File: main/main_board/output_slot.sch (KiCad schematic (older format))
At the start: 5 parts, among them P1 my_pcie_8x

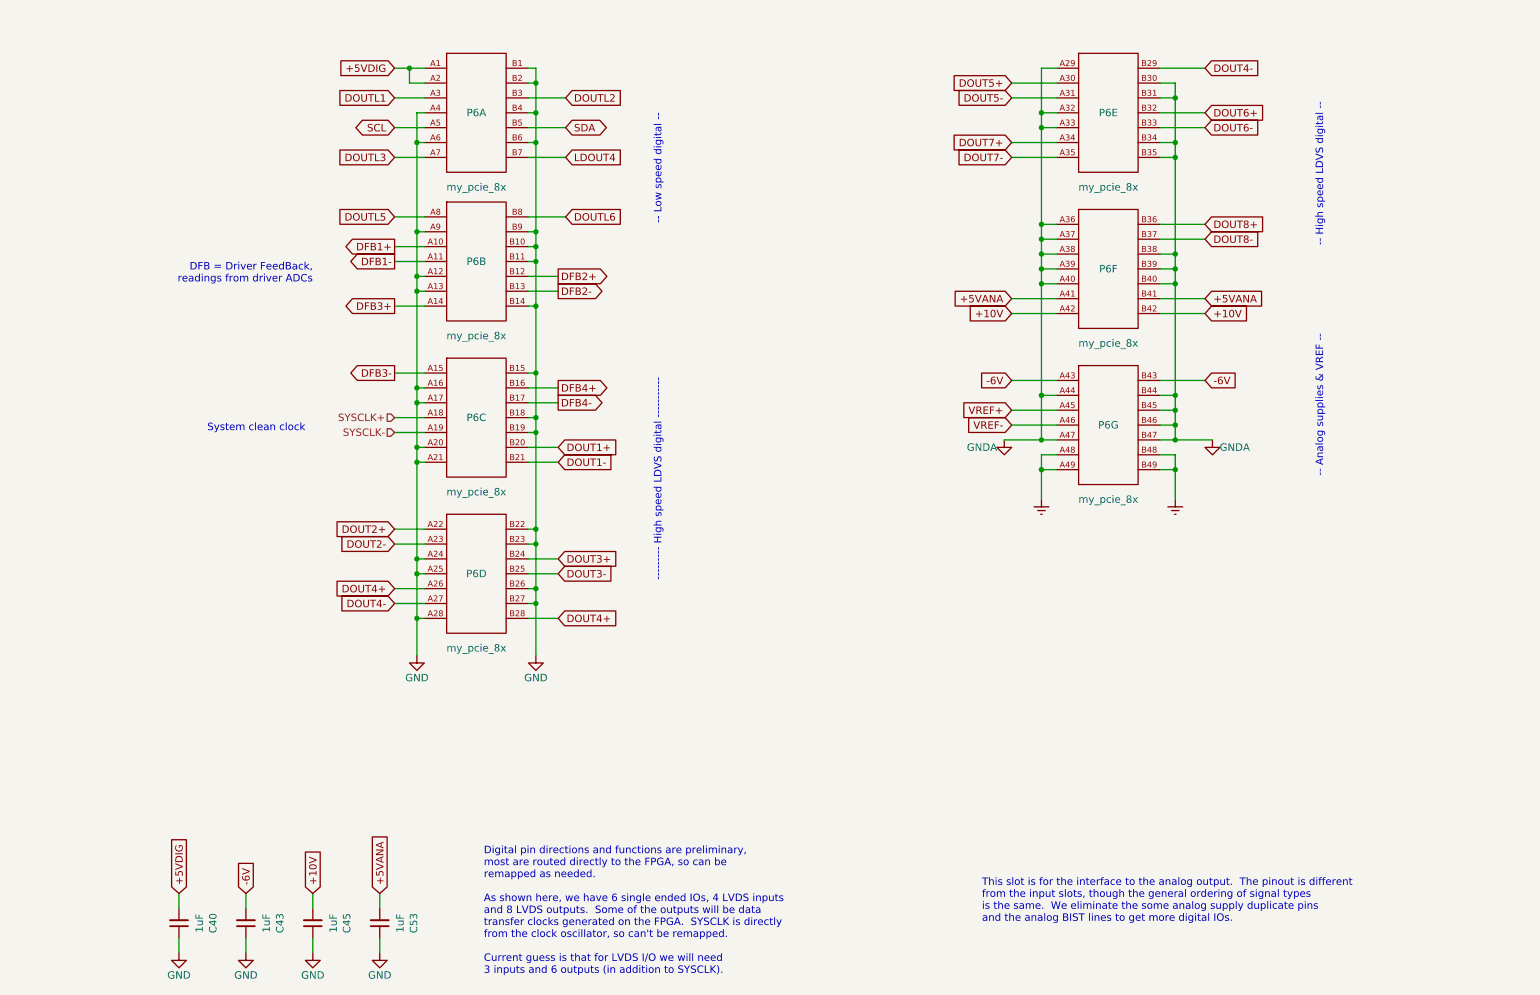
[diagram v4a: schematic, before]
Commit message: Updated for new microzed pin mapping scheme.
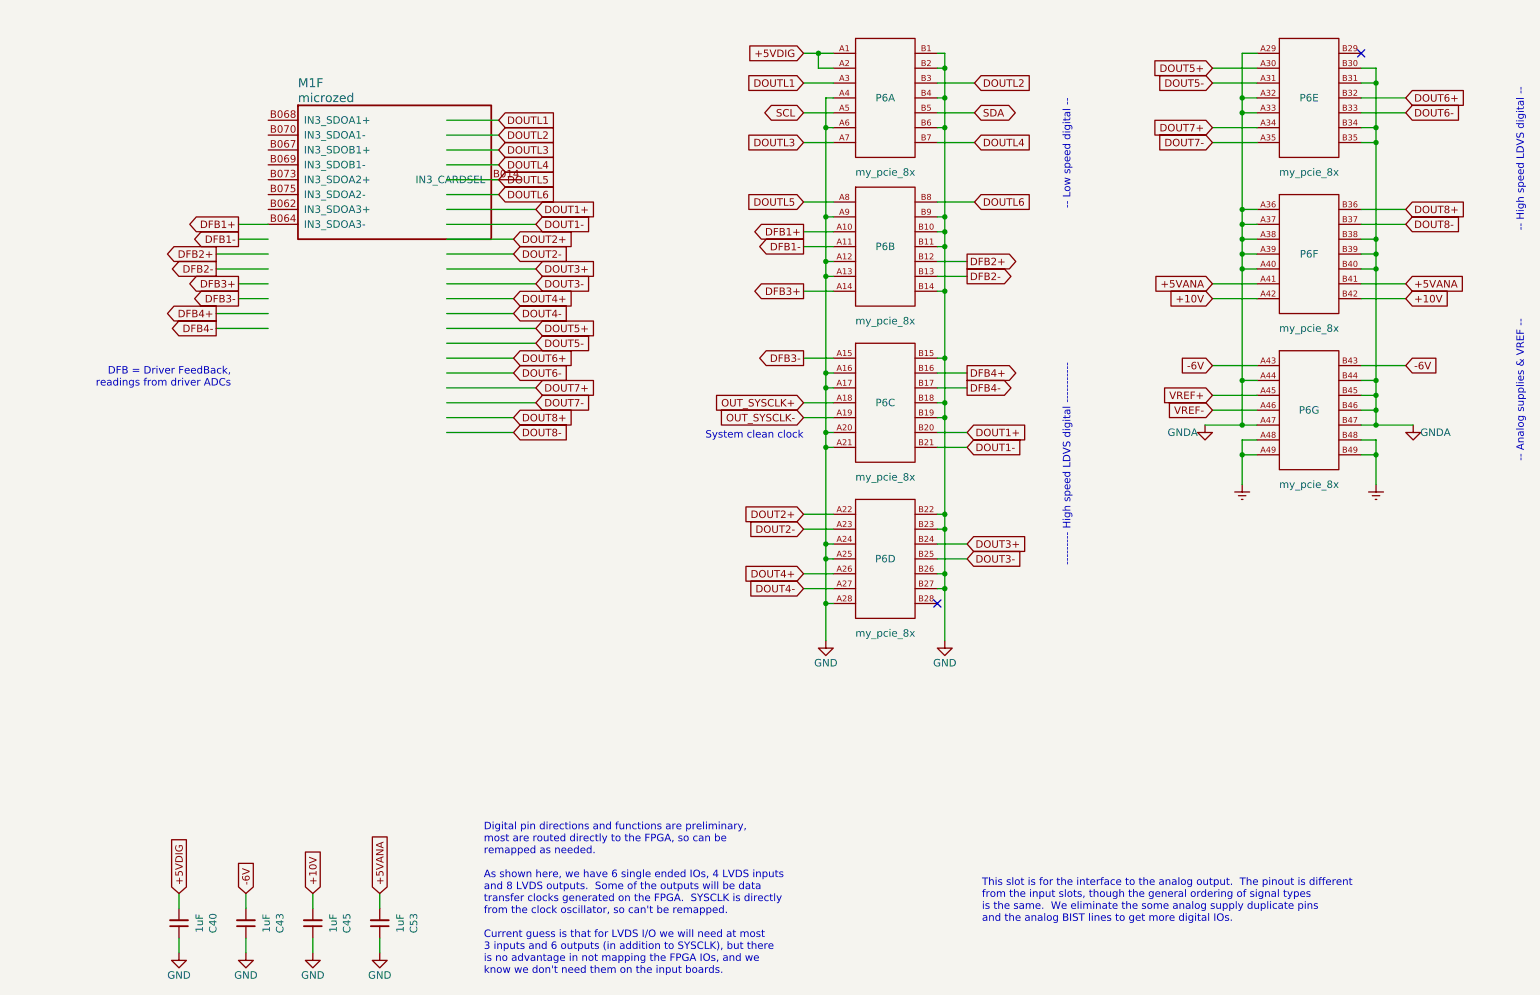
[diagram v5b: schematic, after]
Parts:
- added M1: microzed, main_board:Microzed, symbol microzed:microzed
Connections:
- net labels added: DOUTL4, OUT_SYSCLK+, OUT_SYSCLK-
- net labels removed: LDOUT4, SYSCLK+, SYSCLK-
- wire segments 160 -> 188
- no-connect marks 0 -> 2
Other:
- note added: "Digital pin directions and functions are preliminary,\nmost are routed directly to the FPGA, so can be\nremapped as needed.\n\nAs shown here, we have 6 single ended IOs, 4 LVDS inputs\nand 8 LVDS outputs. Some of the outputs will be data\ntransfer clocks generated on the FPGA. SYSCLK is directly\nfrom the clock oscillator, so can't be remapped.\n\nCurrent guess is that for LVDS I/O we will need a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"
- note removed: "Digital pin directions and functions are preliminary,\nmost are routed directly to the FPGA, so can be\nremapped as needed.\n\nAs shown here, we have 6 single ended IOs, 4 LVDS inputs\nand 8 LVDS outputs. Some of the outputs will be data\ntransfer clocks generated on the FPGA. SYSCLK is directly\nfrom the clock oscillator, so can't be remapped.\n\nCurrent guess is that for LVDS I/O we will need\n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"
- moved on the sheet: P6A, P6B, P6C, P6D, P6E, P6F, P6G

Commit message: Schematic is mostly complete (except for BIST DACs), and passes ERC.  Rough placement of components on PCB.
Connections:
- net labels removed: GNDA
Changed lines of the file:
@@
-$EndComp
-$Comp
-L power:GNDA #PWR0129
-U 1 1 5E2B8A96
-P 10000 3600
-AR Path="/5E525F2C/5E59D3A2/5E2B8A96" Ref="#PWR0129"  Part="1"
-AR Path="/5E525F2C/5E76A42A/5E2B8A96" Ref="#PWR?"  Part="1"
-AR Path="/5E525F2C/5E76E218/5E2B8A96" Ref="#PWR?"  Part="1"
-AR Path="/5E525F2C/5E7721D1/5E2B8A96" Ref="#PWR?"  Part="1"
-AR Path="/5E525FFE/5EBAAEAF/5E2B8A96" Ref="#PWR?"  Part="1"
-AR Path="/5E525FFE/5EBAAF7D/5E2B8A96" Ref="#PWR?"  Part="1"
-AR Path="/5E525FFE/5EBAAF8F/5E2B8A96" Ref="#PWR?"  Part="1"
-AR Path="/5E525FFE/5EBAAFA1/5E2B8A96" Ref="#PWR?"  Part="1"
-AR Path="/5EC15224/5E2B8A96" Ref="#PWR0107"  Part="1"
-F 0 "#PWR0107" H 10000 3350 50  0001 C CNN
-F 1 "GNDA" H 10150 3550 50  0000 C CNN
-F 2 "" H 10000 3600 50  0001 C CNN
-F 3 "" H 10000 3600 50  0001 C CNN
-	1    10000 3600
-	1    0    0    -1
 $EndComp
 $Comp
@@
 Wire Wire Line
 	10000 3600 9750 3600
-$Comp
-L power:GNDA #PWR0161
-U 1 1 5EC152AC
-P 8600 3600
-AR Path="/5E525F2C/5E59D3A2/5EC152AC" Ref="#PWR0161"  Part="1"
-AR Path="/5E525F2C/5E76A42A/5EC152AC" Ref="#PWR?"  Part="1"
-AR Path="/5E525F2C/5E76E218/5EC152AC" Ref="#PWR?"  Part="1"
-AR Path="/5E525F2C/5E7721D1/5EC152AC" Ref="#PWR?"  Part="1"
-AR Path="/5E525FFE/5EBAAEAF/5EC152AC" Ref="#PWR?"  Part="1"
-AR Path="/5E525FFE/5EBAAF7D/5EC152AC" Ref="#PWR?"  Part="1"
-AR Path="/5E525FFE/5EBAAF8F/5EC152AC" Ref="#PWR?"  Part="1"
-AR Path="/5E525FFE/5EBAAFA1/5EC152AC" Ref="#PWR?"  Part="1"
-AR Path="/5EC15224/5EC152AC" Ref="#PWR0104"  Part="1"
-F 0 "#PWR0104" H 8600 3350 50  0001 C CNN
-F 1 "GNDA" H 8450 3550 50  0000 C CNN
-F 2 "" H 8600 3600 50  0001 C CNN
-F 3 "" H 8600 3600 50  0001 C CNN
-	1    8600 3600
-	1    0    0    -1
-$EndComp
 Wire Wire Line
 	8600 3600 8850 3600
@@
 Text GLabel 5900 3550 0    50   Input ~ 0
 OUT_SYSCLK-
+$Comp
+L power:GND #PWR?
+U 1 1 5F698B42
+P 8600 3600
+AR Path="/5E525F2C/5E59D3A2/5F698B42" Ref="#PWR?"  Part="1"
+AR Path="/5E525F2C/5E76A42A/5F698B42" Ref="#PWR?"  Part="1"
+AR Path="/5E525F2C/5E76E218/5F698B42" Ref="#PWR?"  Part="1"
+AR Path="/5E525F2C/5E7721D1/5F698B42" Ref="#PWR?"  Part="1"
+AR Path="/5E525FFE/5EBAAEAF/5F698B42" Ref="#PWR?"  Part="1"
+AR Path="/5E525FFE/5EBAAF7D/5F698B42" Ref="#PWR?"  Part="1"
+AR Path="/5E525FFE/5EBAAF8F/5F698B42" Ref="#PWR?"  Part="1"
+AR Path="/5E525FFE/5EBAAFA1/5F698B42" Ref="#PWR?"  Part="1"
+AR Path="/5EC15224/5F698B42" Ref="#PWR0118"  Part="1"
+F 0 "#PWR0118" H 8600 3350 50  0001 C CNN
+F 1 "GND" H 8600 3450 50  0000 C CNN
+F 2 "" H 8600 3600 50  0001 C CNN
+F 3 "" H 8600 3600 50  0001 C CNN
+	1    8600 3600
+	1    0    0    -1
+$EndComp
+$Comp
+L power:GND #PWR?
+U 1 1 5F698E9C
+P 10000 3600
+AR Path="/5E525F2C/5E59D3A2/5F698E9C" Ref="#PWR?"  Part="1"
+AR Path="/5E525F2C/5E76A42A/5F698E9C" Ref="#PWR?"  Part="1"
+AR Path="/5E525F2C/5E76E218/5F698E9C" Ref="#PWR?"  Part="1"
+AR Path="/5E525F2C/5E7721D1/5F698E9C" Ref="#PWR?"  Part="1"
+AR Path="/5E525FFE/5EBAAEAF/5F698E9C" Ref="#PWR?"  Part="1"
+AR Path="/5E525FFE/5EBAAF7D/5F698E9C" Ref="#PWR?"  Part="1"
+AR Path="/5E525FFE/5EBAAF8F/5F698E9C" Ref="#PWR?"  Part="1"
+AR Path="/5E525FFE/5EBAAFA1/5F698E9C" Ref="#PWR?"  Part="1"
+AR Path="/5EC15224/5F698E9C" Ref="#PWR0119"  Part="1"
+F 0 "#PWR0119" H 10000 3350 50  0001 C CNN
+F 1 "GND" H 10000 3450 50  0000 C CNN
+F 2 "" H 10000 3600 50  0001 C CNN
+F 3 "" H 10000 3600 50  0001 C CNN
+	1    10000 3600
+	1    0    0    -1
+$EndComp
 $EndSCHEMATC

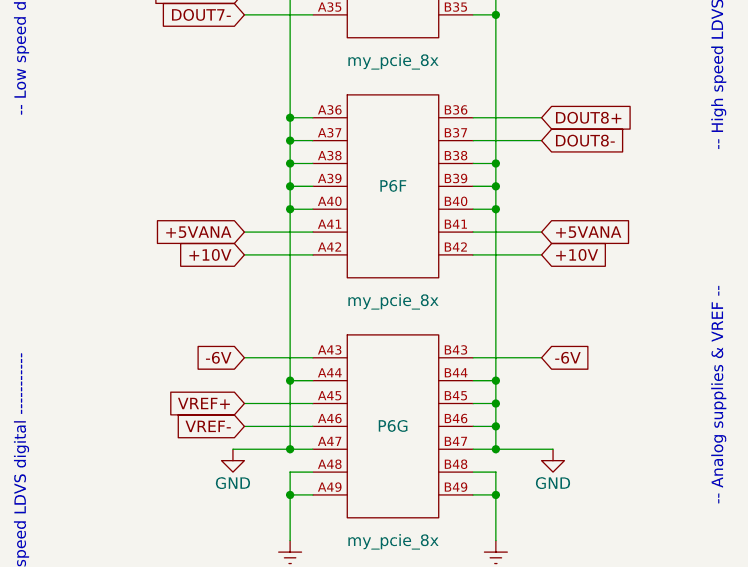
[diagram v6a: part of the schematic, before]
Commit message: Mostly work on main board layout. Aligned things on mm grid for easier routing, moved things around to create routing area. Neatened up component groups onto the grid. Parts of the routing plan are now drawn on the PCB.  See also notebook.txt. Reduced pad size of the PCIE connector, tweaked design rule clearances. Minor schematic tweaks.
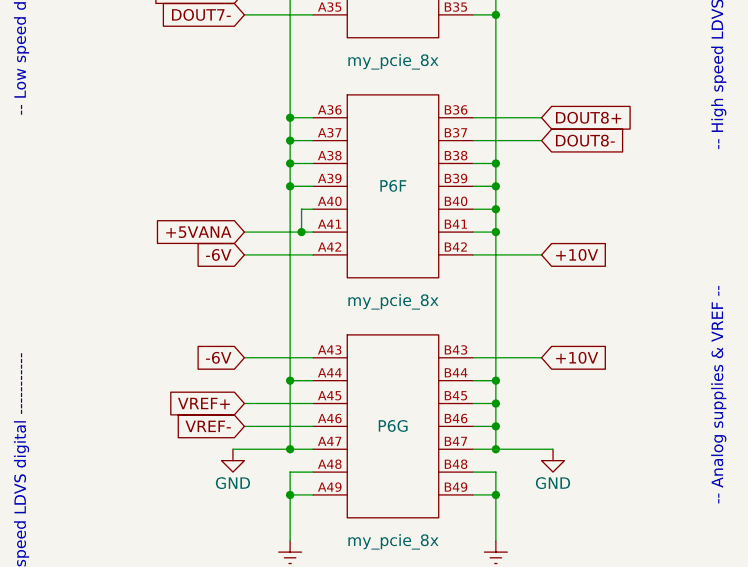
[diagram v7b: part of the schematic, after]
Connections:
- wire segments 188 -> 190
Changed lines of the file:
@@
 Text GLabel 8650 3500 0    50   Input ~ 0
 VREF-
-Text GLabel 9950 2650 2    50   Input ~ 0
-+5VANA
 Text GLabel 9950 2750 2    50   Input ~ 0
 +10V
-Text GLabel 9950 3200 2    50   Input ~ 0
+Text GLabel 8650 2750 0    50   Input ~ 0
 -6V
 Text GLabel 7050 1500 2    50   BiDi ~ 0
@@
 Text GLabel 8650 3200 0    50   Input ~ 0
 -6V
-Text GLabel 8650 2750 0    50   Input ~ 0
+Text GLabel 9950 3200 2    50   Input ~ 0
 +10V
-Wire Wire Line
-	9950 2650 9650 2650
 Text GLabel 8650 2650 0    50   Input ~ 0
 +5VANA
 Wire Wire Line
-	8950 2650 8650 2650
+	8950 2650 8900 2650
 Wire Wire Line
 	9650 1700 9750 1700
@@
 Connection ~ 8850 2450
 Wire Wire Line
-	8850 2450 8850 2550
-Wire Wire Line
-	8950 2550 8850 2550
-Connection ~ 8850 2550
-Wire Wire Line
-	8850 2550 8850 3300
-Wire Wire Line
 	9650 2350 9750 2350
 Connection ~ 9750 2350
@@
 Connection ~ 9750 2550
 Wire Wire Line
-	9750 2550 9750 3300
+	9750 2550 9750 2650
 Text Notes 10750 2300 1    50   ~ 0
 -- High speed LDVS digital --
@@
 	1    0    0    -1
 $EndComp
+Wire Wire Line
+	8850 2450 8850 3300
+Wire Wire Line
+	8950 2550 8900 2550
+Wire Wire Line
+	8900 2550 8900 2650
+Connection ~ 8900 2650
+Wire Wire Line
+	8900 2650 8650 2650
+Wire Wire Line
+	9650 2650 9750 2650
+Connection ~ 9750 2650
+Wire Wire Line
+	9750 2650 9750 3300
 $EndSCHEMATC

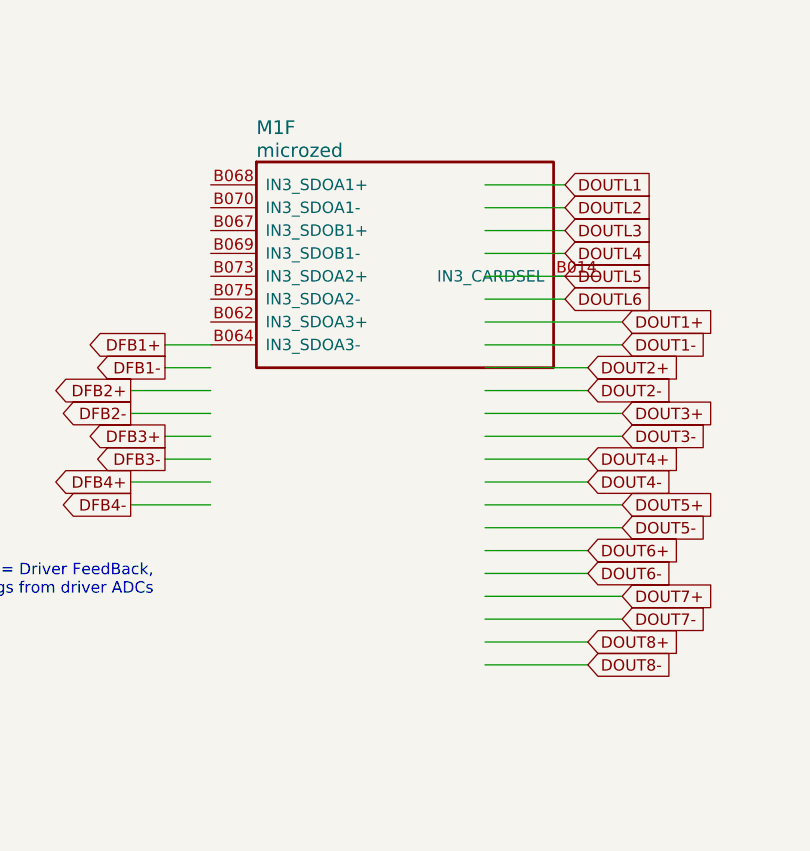
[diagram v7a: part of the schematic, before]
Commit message: Changes related to pin mapping. There's a new BIST unit in the Microzed symbol, and the unit ordering has changed. I also added SDI lines to the input slots which could be used to configure the ADC in a future version of the input board. Added some wire labels for easier routing.
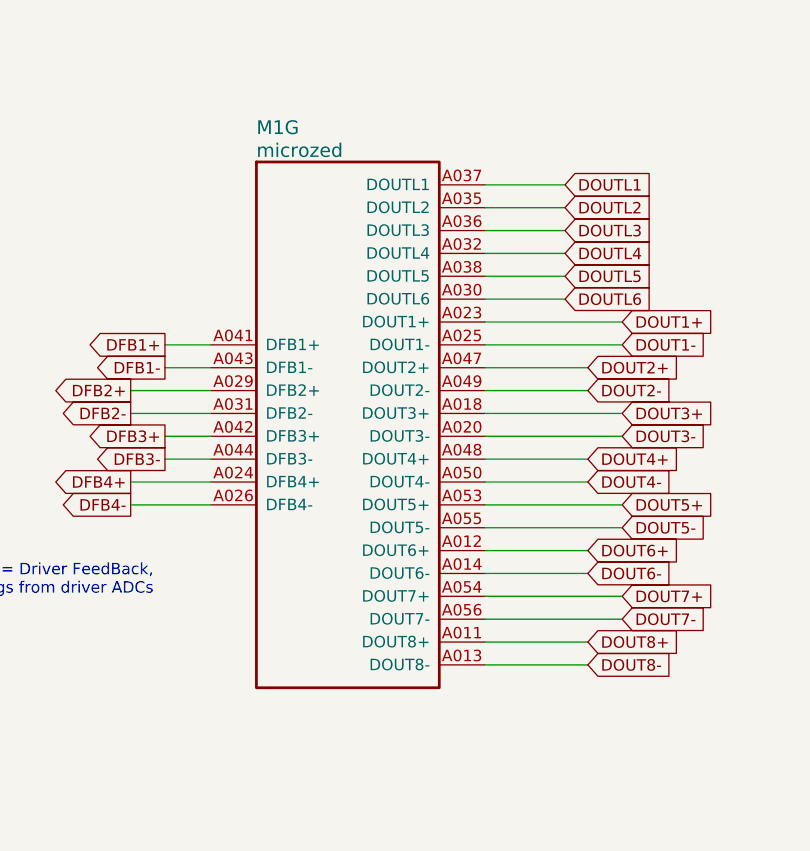
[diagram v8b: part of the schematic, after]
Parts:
- removed M1: microzed, main_board:Microzed, symbol microzed:microzed
- added M1: microzed, main_board:Microzed, symbol microzed:microzed
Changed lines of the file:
@@
 NoConn ~ 9650 1100
 NoConn ~ 6800 4800
-$Comp
-L microzed:microzed M1
-U 6 1 5EE73154
-P 2300 1550
-F 0 "M1" H 2500 1800 60  0000 L CNN
-F 1 "microzed" H 2500 1700 60  0000 L CNN
-F 2 "main_board:Microzed" H 2500 1600 60  0001 L CNN
-F 3 "" H 2500 1400 60  0001 L CNN
-	6    2300 1550
-	1    0    0    -1
-$EndComp
 Wire Wire Line
 	2100 2250 2300 2250
@@
 Wire Wire Line
 	9750 2650 9750 3300
+$Comp
+L microzed:microzed M1
+U 7 1 5F1DB65F
+P 2300 1550
+F 0 "M1" H 2500 1800 60  0000 L CNN
+F 1 "microzed" H 2500 1700 60  0000 L CNN
+F 2 "main_board:Microzed" H 2500 1600 60  0001 L CNN
+F 3 "" H 2500 1400 60  0001 L CNN
+	7    2300 1550
+	1    0    0    -1
+$EndComp
 $EndSCHEMATC
